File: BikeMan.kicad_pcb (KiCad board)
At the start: 2 copper layers, 78 parts, among them J1 USB_A_stacked, J10 HDMI_A_1.4, J2 USB_A_stacked, J4 Barrel_Jack, J5 PushConnector_8pos, J6 PushConnector_8pos, J7 PushConnector_8pos, J8 MagJack, J9 Micro_SD_Card_Det, Q1 AUIRF7316QTR, Q2 AUIRF7316QTR, Q3 AUIRF7316QTR, Q4 AUIRF7316QTR, U1 MCP2515, U2 MCP2551, U3 AP64501, U4 RT9742GGJ5, U5 NPIC6C596ADJ, U6 PCF8574DWR, U7 PCF85063A, U8 TUSB2046IBVF

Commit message: Added Daughter Card
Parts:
- removed R18, R19, R20, R21, R22, R23, R24, R25, R26, R27, R28, R29, R30, R31, R32, R33, R34, R35, R36, R37, R38: R, Resistor_SMD:R_0805_2012Metric
- removed U7: PCF85063A, Package_SO:SOIC-8_3.9x4.9mm_P1.27mm
- added H1: MountingHole_Pad, MountingHole:MountingHole_3.2mm_M3, F.Cu at (59.7, 38.1)
- added H2: MountingHole_Pad, MountingHole:MountingHole_3.2mm_M3, F.Cu at (203.2, 38.1)
- added H3: MountingHole_Pad, MountingHole:MountingHole_3.2mm_M3, F.Cu at (203.2, 152.4)
- added H4: MountingHole_Pad, MountingHole:MountingHole_3.2mm_M3, F.Cu at (59.7, 152.4)
- added J11: ExpansionSlotA, Connector_PinSocket_2.54mm:PinSocket_2x03_P2.54mm_Vertical, F.Cu at (128.3, 111.8)
- added J12: ExpansionSlotB, Connector_PinSocket_2.54mm:PinSocket_2x03_P2.54mm_Vertical, F.Cu at (87.6, 78.7)
- added J13: ExpansionSlotC, Connector_PinSocket_2.54mm:PinSocket_2x03_P2.54mm_Vertical, F.Cu at (128.3, 83.8)
- added J14: CAN_{OUT}, Connector_Molex:Molex_Micro-Fit_3.0_43045-0412_2x02_P3.00mm_Vertical, F.Cu at (66.0, 95.2)
- added J3: CAN_{IN}, Connector_Molex:Molex_Micro-Fit_3.0_43045-0412_2x02_P3.00mm_Vertical, F.Cu at (66.0, 83.6)
- added JP2: Jumper, Connector_PinHeader_2.54mm:PinHeader_1x02_P2.54mm_Vertical, F.Cu at (63.7, 69.5)
- J5: value PushConnector_8pos -> GPIO Outputs
- J6: value PushConnector_8pos -> GPIO Inputs
- J7: value PushConnector_8pos -> CAN / Power / GND
- R1, R2: moved to B.Cu
- R15, R16, R17: value R -> CTS-766161102GP; footprint Resistor_SMD:R_0805_2012Metric -> Package_SO:SOIC-16_3.9x9.9mm_P1.27mm; moved to B.Cu
- moved C8 283.9 mm to (79.2, 132.0)
- moved U3 283.9 mm to (71.6, 130.7)
- moved C7 276.8 mm to (79.2, 128.2)
- moved J4 275.7 mm to (71.1, 144.7)
- moved U1 241.4 mm to (78.7, 58.4), turned to -90 degrees
- moved R5 235.9 mm to (106.7, 54.6), turned to -90 degrees
- moved U2 234.6 mm to (99.7, 57.7), turned to -90 degrees
- moved JP1 228.6 mm to (108.0, 59.7), turned to 90 degrees
- moved JP4 184.4 mm to (73.5, 122.7)
- moved BT1 165.3 mm to (194.3, 81.3), turned to 90 degrees
- moved R4 154.4 mm to (68.6, 69.8), turned to -90 degrees
- moved D3 153.4 mm to (194.3, 96.5), turned to -90 degrees
- moved TP1 151.7 mm to (64.8, 59.7), turned to -90 degrees
- moved C2 140.3 mm to (91.4, 56.6), turned to 180 degrees
- moved R3 121.7 mm to (91.4, 61.0), turned to 180 degrees
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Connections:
- net /CAN_{H}_1 renamed /CAN_{H}
- net /CAN_{L}_1 renamed /CAN_{L}
- J8 pad 1: no_connect_196 -> no_connect_209
- J8 pad 8: no_connect_198 -> no_connect_211
- Module1 pad 10: no_connect_199 -> no_connect_212
- Module1 pad 102: no_connect_200 -> no_connect_213
- Module1 pad 104: no_connect_201 -> no_connect_214
- Module1 pad 106: no_connect_202 -> no_connect_215
- Module1 pad 109: no_connect_203 -> no_connect_216
- Module1 pad 110: no_connect_204 -> no_connect_217
- Module1 pad 111: no_connect_205 -> no_connect_218
- Module1 pad 112: no_connect_206 -> no_connect_219
- Module1 pad 115: no_connect_207 -> no_connect_220
- Module1 pad 116: no_connect_208 -> no_connect_221
- Module1 pad 117: no_connect_209 -> no_connect_222
- Module1 pad 118: no_connect_210 -> no_connect_223
- Module1 pad 12: no_connect_211 -> no_connect_224
- Module1 pad 121: no_connect_212 -> no_connect_225
- Module1 pad 122: no_connect_213 -> no_connect_226
- Module1 pad 123: no_connect_214 -> no_connect_227
- Module1 pad 124: no_connect_215 -> no_connect_228
- Module1 pad 127: no_connect_216 -> no_connect_229
- Module1 pad 128: no_connect_217 -> no_connect_230
- Module1 pad 129: no_connect_218 -> no_connect_231
- Module1 pad 130: no_connect_219 -> no_connect_232
- Module1 pad 133: no_connect_220 -> no_connect_233
- Module1 pad 134: no_connect_221 -> no_connect_234
- Module1 pad 135: no_connect_222 -> no_connect_235
- Module1 pad 136: no_connect_223 -> no_connect_236
- Module1 pad 139: no_connect_224 -> no_connect_237
- Module1 pad 140: no_connect_225 -> no_connect_238
- Module1 pad 141: no_connect_226 -> no_connect_239
- Module1 pad 142: no_connect_227 -> no_connect_240
- Module1 pad 143: no_connect_228 -> no_connect_241
- Module1 pad 145: no_connect_229 -> no_connect_242
- Module1 pad 146: no_connect_230 -> no_connect_243
- Module1 pad 147: no_connect_231 -> no_connect_244
- Module1 pad 148: no_connect_232 -> no_connect_245
- Module1 pad 149: no_connect_233 -> no_connect_246
- Module1 pad 152: no_connect_234 -> no_connect_247
- Module1 pad 154: no_connect_235 -> no_connect_248
- Module1 pad 157: no_connect_236 -> no_connect_249
- Module1 pad 158: no_connect_237 -> no_connect_250
- Module1 pad 159: no_connect_238 -> no_connect_251
- Module1 pad 160: no_connect_239 -> no_connect_252
- Module1 pad 163: no_connect_240 -> no_connect_253
- Module1 pad 164: no_connect_241 -> no_connect_254
- Module1 pad 165: no_connect_242 -> no_connect_255
- Module1 pad 166: no_connect_243 -> no_connect_256
- Module1 pad 169: no_connect_244 -> no_connect_257
- Module1 pad 171: no_connect_245 -> no_connect_258
- Module1 pad 175: no_connect_246 -> no_connect_259
- Module1 pad 177: no_connect_247 -> no_connect_260
- Module1 pad 181: no_connect_248 -> no_connect_261
- Module1 pad 183: no_connect_249 -> no_connect_262
- Module1 pad 187: no_connect_250 -> no_connect_263
- Module1 pad 189: no_connect_251 -> no_connect_264
- Module1 pad 19: no_connect_252 -> no_connect_265
- Module1 pad 193: no_connect_253 -> no_connect_266
- Module1 pad 195: no_connect_254 -> no_connect_267
- Module1 pad 3: no_connect_255 -> no_connect_268
- Module1 pad 5: no_connect_256 -> no_connect_269
- R15 pad 2: /GPIO/I_{1} -> Net-(R15-Pad16)
- R16 pad 1: /GPIO/I_{1} -> /GPIO/I_{3}
- R16 pad 2: GND -> /Input_{4}
- R17 pad 1: /Input_{2} -> +12V
- R17 pad 2: /GPIO/I_{2} -> +12V
- U1 pad 10: no_connect_257 -> no_connect_270
- U1 pad 11: no_connect_258 -> no_connect_271
- U1 pad 3: no_connect_259 -> no_connect_272
- U1 pad 4: no_connect_260 -> no_connect_273
- U1 pad 5: no_connect_261 -> no_connect_274
- U1 pad 6: no_connect_262 -> no_connect_275
- U2 pad 5: no_connect_263 -> no_connect_276
- U5 pad 9: no_connect_264 -> no_connect_277
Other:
- board outline added: 152.4 x 127 mm
- board text added: "Daughter Card"

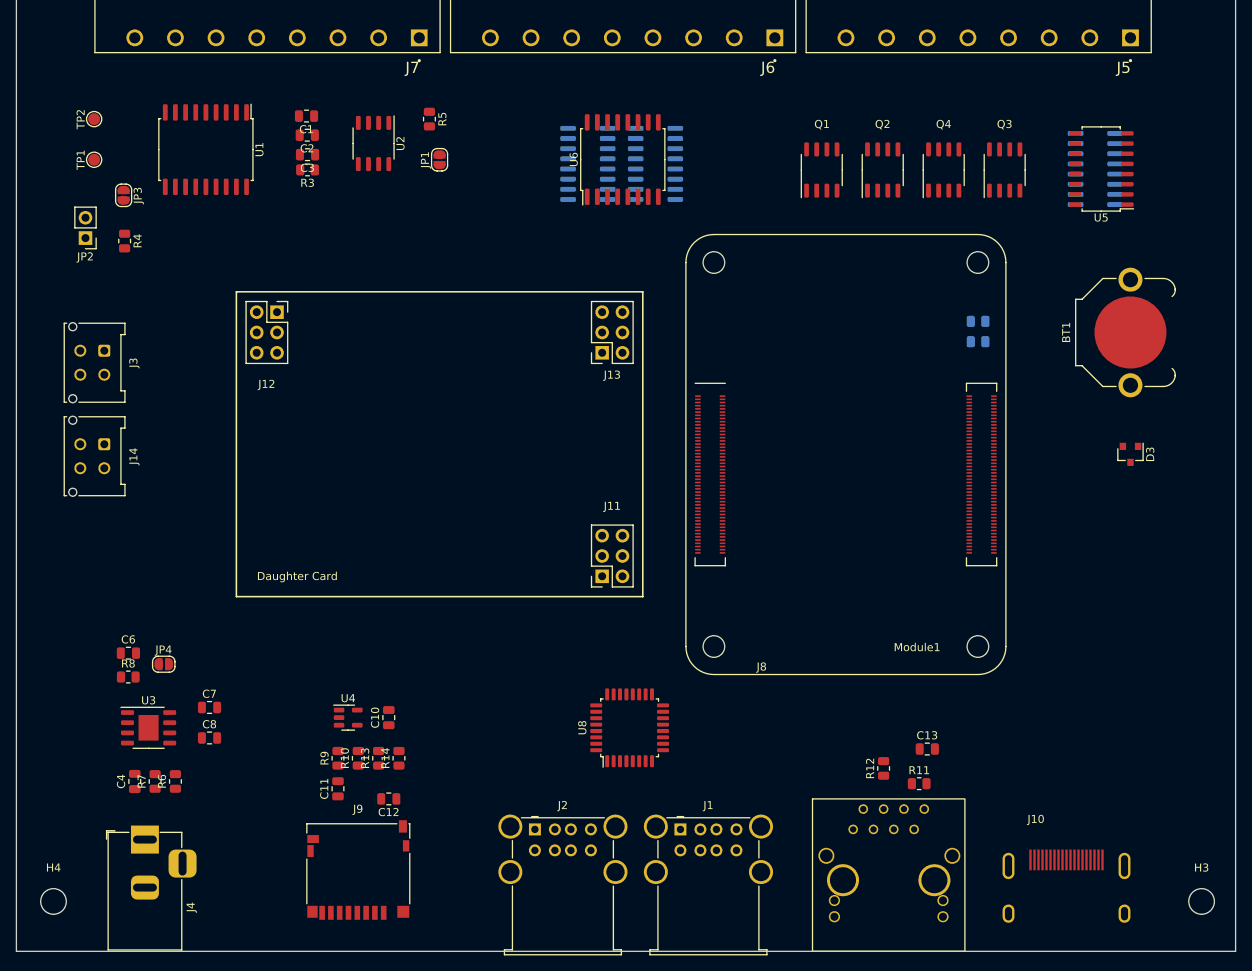
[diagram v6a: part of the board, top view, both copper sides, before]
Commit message: more layout: power supply and gpio
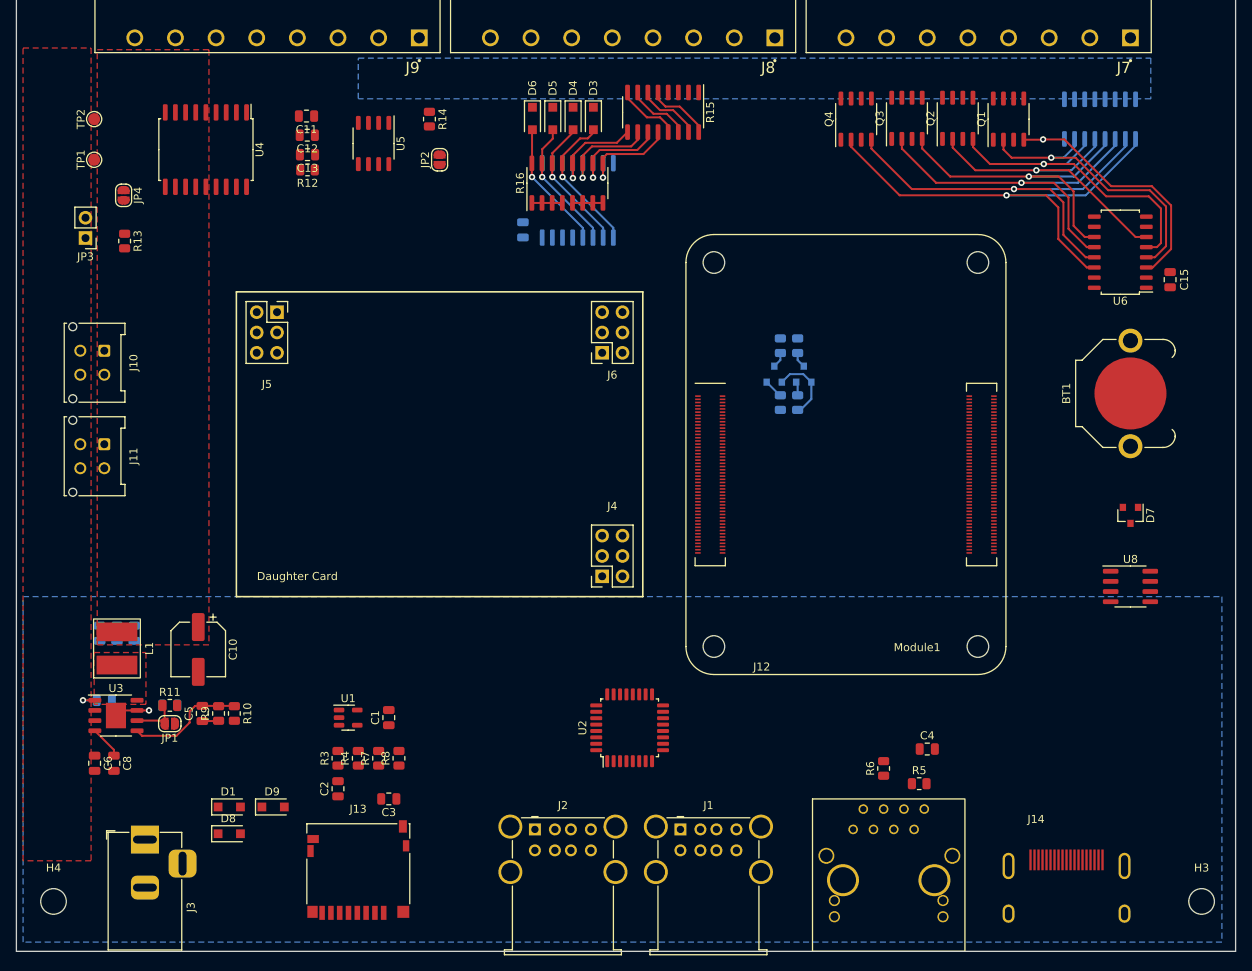
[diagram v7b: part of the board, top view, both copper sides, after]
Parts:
- added C10: 100uF, Capacitor_SMD:CP_Elec_6.3x5.9, F.Cu at (77.8, 120.9)
- added C14: C, Capacitor_SMD:C_0805_2012Metric, B.Cu at (118.4, 68.5)
- added C15: C, Capacitor_SMD:C_0805_2012Metric, F.Cu at (199.3, 74.7)
- added C16: 10uF, Capacitor_SMD:C_0805_2012Metric, B.Cu at (67.6, 118.9)
- added C17: 10uF, Capacitor_SMD:C_0805_2012Metric, B.Cu at (69.8, 118.9)
- added C18: 10uF, Capacitor_SMD:C_0805_2012Metric, B.Cu at (65.5, 118.9)
- added C6: 10uF, Capacitor_SMD:C_0805_2012Metric, F.Cu at (64.8, 135.1)
- added D1: Diode, Diode_SMD:D_SOD-123F, F.Cu at (81.7, 140.6)
- added D3: Diode, Diode_SMD:D_SOD-123F, F.Cu at (127.2, 54.5)
- added D4: Diode, Diode_SMD:D_SOD-123F, F.Cu at (124.6, 54.5)
- added D5: Diode, Diode_SMD:D_SOD-123F, F.Cu at (122.1, 54.5)
- added D6: Diode, Diode_SMD:D_SOD-123F, F.Cu at (119.6, 54.5)
- added D8: Diode, Diode_SMD:D_SOD-123F, F.Cu at (81.7, 143.9)
- added D9: Diode, Diode_SMD:D_SOD-123F, F.Cu at (87.1, 140.6)
- added L1: 3.3uH, Custom-Footprints:Bourns SRN6045Y Inductor, F.Cu at (67.6, 120.8)
- added Q5: DMN62D0U-7, Package_TO_SOT_SMD:SOT-23, B.Cu at (153.5, 86.5)
- added Q6: DMN62D0U-7, Package_TO_SOT_SMD:SOT-23, B.Cu at (149.8, 86.5)
- added R18: R, Resistor_SMD:R_0805_2012Metric, B.Cu at (152.7, 90.0)
- added R19: R, Resistor_SMD:R_0805_2012Metric, B.Cu at (150.5, 90.0)
- added U8: PCF85063A, Package_SO:SOIC-8_3.9x4.9mm_P1.27mm, F.Cu at (194.3, 113.0)
- C7: renamed from C6; moved to B.Cu
- C8: renamed from C7; value C -> 10nF
- C9: renamed from C8; value C -> 100nF; moved to B.Cu
- J10: renamed from J3; value CAN_{IN} -> Conn_01x04_Female
- J11: renamed from J14; value CAN_{OUT} -> Conn_01x04_Female
- J4: renamed from J11; value ExpansionSlotA -> Conn_01x06_Female
- J5: renamed from J12; value ExpansionSlotB -> Conn_01x06_Female
- J6: renamed from J13; value ExpansionSlotC -> Conn_01x06_Female
- J7: renamed from J5; value GPIO Outputs -> PushConnector_8pos
- J8: renamed from J6; value GPIO Inputs -> PushConnector_8pos
- J9: renamed from J7; value CAN / Power / GND -> PushConnector_8pos
- R15, R16: moved to F.Cu
- U7: renamed from U6; moved to B.Cu
- moved R2 24.7 mm to (150.5, 82.9), turned to -90 degrees
- moved Q1 24.2 mm to (179.1, 54.6)
- moved R1 22.8 mm to (152.7, 82.9), turned to -90 degrees
- moved C9 14.0 mm to (66.0, 127.3)
- moved C8 13.8 mm to (67.2, 135.1), turned to -90 degrees
- moved Q3 13.8 mm to (166.4, 54.5)
- moved R10 13.1 mm to (82.3, 128.9), turned to -90 degrees
- moved Q4 12.7 mm to (160.0, 54.6)
- moved C5 12.0 mm to (78.3, 128.9)
- moved Q2 11.4 mm to (172.7, 54.5)
- moved U6 10.7 mm to (193.0, 71.2)
- moved R9 10.1 mm to (80.3, 128.9)
- moved C7 8.33 mm to (74.2, 127.9), turned to 180 degrees
- moved BT1 7.62 mm to (194.3, 88.9)
- moved D7 7.62 mm to (194.3, 104.1)
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- renumbered C10 to C1, C1 to C11, C2 to C12, C3 to C13, C11 to C2, C12 to C3, C13 to C4, C4 to C5, D3 to D7, J8 to J12, J9 to J13, J10 to J14, J4 to J3, JP4 to JP1, JP1 to JP2, JP2 to JP3, JP3 to JP4, R7 to R10, R8 to R11, R3 to R12, R4 to R13, R5 to R14, R9 to R3, R10 to R4, R11 to R5, R12 to R6, R13 to R7, R14 to R8, R6 to R9, U4 to U1, U8 to U2, U1 to U4, U2 to U5, U5 to U6
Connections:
- net Net-(C8-Pad2) renamed /Power/SW
- net no_connect_206 renamed no_connect_210
- H1 pad 1: no_connect_205 -> no_connect_209
- H3 pad 1: no_connect_207 -> no_connect_211
- H4 pad 1: no_connect_208 -> no_connect_212
- J12 pad 1: no_connect_209 -> no_connect_213
- J12 pad 8: no_connect_211 -> no_connect_215
- J4 pad 4: /SCL -> /SDA_{5V}
- J4 pad 5: /SDA -> /SCL_{5V}
- Module1 pad 10: no_connect_212 -> no_connect_216
- Module1 pad 102: no_connect_213 -> no_connect_217
- Module1 pad 104: no_connect_214 -> no_connect_218
- Module1 pad 106: no_connect_215 -> no_connect_219
- Module1 pad 109: no_connect_216 -> no_connect_220
- Module1 pad 110: no_connect_217 -> no_connect_221
- Module1 pad 111: no_connect_218 -> no_connect_222
- Module1 pad 112: no_connect_219 -> no_connect_223
- Module1 pad 115: no_connect_220 -> no_connect_224
- Module1 pad 116: no_connect_221 -> no_connect_225
- Module1 pad 117: no_connect_222 -> no_connect_226
- Module1 pad 118: no_connect_223 -> no_connect_227
- Module1 pad 12: no_connect_224 -> no_connect_228
- Module1 pad 121: no_connect_225 -> no_connect_229
- Module1 pad 122: no_connect_226 -> no_connect_230
- Module1 pad 123: no_connect_227 -> no_connect_231
- Module1 pad 124: no_connect_228 -> no_connect_232
- Module1 pad 127: no_connect_229 -> no_connect_233
- Module1 pad 128: no_connect_230 -> no_connect_234
- Module1 pad 129: no_connect_231 -> no_connect_235
- Module1 pad 130: no_connect_232 -> no_connect_236
- Module1 pad 133: no_connect_233 -> no_connect_237
- Module1 pad 134: no_connect_234 -> no_connect_238
- Module1 pad 135: no_connect_235 -> no_connect_239
- Module1 pad 136: no_connect_236 -> no_connect_240
- Module1 pad 139: no_connect_237 -> no_connect_241
- Module1 pad 140: no_connect_238 -> no_connect_242
- Module1 pad 141: no_connect_239 -> no_connect_243
- Module1 pad 142: no_connect_240 -> no_connect_244
- Module1 pad 143: no_connect_241 -> no_connect_245
- Module1 pad 145: no_connect_242 -> no_connect_246
- Module1 pad 146: no_connect_243 -> no_connect_247
- Module1 pad 147: no_connect_244 -> no_connect_248
- Module1 pad 148: no_connect_245 -> no_connect_249
- Module1 pad 149: no_connect_246 -> no_connect_250
- Module1 pad 152: no_connect_247 -> no_connect_251
- Module1 pad 154: no_connect_248 -> no_connect_252
- Module1 pad 157: no_connect_249 -> no_connect_253
- Module1 pad 158: no_connect_250 -> no_connect_254
- Module1 pad 159: no_connect_251 -> no_connect_255
- Module1 pad 160: no_connect_252 -> no_connect_256
- Module1 pad 163: no_connect_253 -> no_connect_257
- Module1 pad 164: no_connect_254 -> no_connect_258
- Module1 pad 165: no_connect_255 -> no_connect_259
- Module1 pad 166: no_connect_256 -> no_connect_260
- Module1 pad 169: no_connect_257 -> no_connect_261
- Module1 pad 171: no_connect_258 -> no_connect_262
- Module1 pad 175: no_connect_259 -> no_connect_263
- Module1 pad 177: no_connect_260 -> no_connect_264
- Module1 pad 181: no_connect_261 -> no_connect_265
- Module1 pad 183: no_connect_262 -> no_connect_266
- Module1 pad 187: no_connect_263 -> no_connect_267
- Module1 pad 189: no_connect_264 -> no_connect_268
- Module1 pad 19: no_connect_265 -> no_connect_269
- Module1 pad 193: no_connect_266 -> no_connect_270
- Module1 pad 195: no_connect_267 -> no_connect_271
- Module1 pad 3: no_connect_268 -> no_connect_272
- Module1 pad 5: no_connect_269 -> no_connect_273
- Module1 pad 80: /SCL -> /SCL_{3.3V}
- Module1 pad 82: /SDA -> /SDA_{3.3V}
- Q1 pad 2: /GPIO/OUT_CTL_{1} -> /GPIO/OUT_CTL_{2}
- Q1 pad 4: /GPIO/OUT_CTL_{2} -> /GPIO/OUT_CTL_{1}
- Q1 pad 5: /OUT_{2} -> /OUT_{1}
- Q1 pad 7: /OUT_{1} -> /OUT_{2}
- Q2 pad 2: /GPIO/OUT_CTL_{3} -> /GPIO/OUT_CTL_{4}
- Q2 pad 4: /GPIO/OUT_CTL_{4} -> /GPIO/OUT_CTL_{3}
- Q2 pad 5: /OUT_{4} -> /OUT_{3}
- Q2 pad 7: /OUT_{3} -> /OUT_{4}
- Q3 pad 2: /GPIO/OUT_CTL_{5} -> /GPIO/OUT_CTL_{6}
- Q3 pad 4: /GPIO/OUT_CTL_{6} -> /GPIO/OUT_CTL_{5}
- Q3 pad 5: /OUT_{6} -> /OUT_{5}
- Q3 pad 7: /OUT_{5} -> /OUT_{6}
- Q4 pad 2: /GPIO/OUT_CTL_{7} -> /GPIO/OUT_CTL_{8}
- Q4 pad 4: /GPIO/OUT_CTL_{8} -> /GPIO/OUT_CTL_{7}
- Q4 pad 5: /OUT_{8} -> /OUT_{7}
- Q4 pad 7: /OUT_{7} -> /OUT_{8}
- R1 pad 1: +3V3 -> +5V
- R1 pad 2: /SDA -> /SDA_{5V}
- R15 pad 10: Net-(R15-Pad10) -> /GPIO/I_{3}
- R15 pad 11: GND -> /GPIO/I_{2}
- R15 pad 12: /GPIO/I_{2} -> /GPIO/I_{1}
- R15 pad 14: GND -> Net-(R15-Pad14)
- R15 pad 15: /GPIO/I_{1} -> Net-(R15-Pad15)
- R15 pad 2: Net-(R15-Pad16) -> /Input_{2}
- R15 pad 3: /GPIO/I_{1} -> /Input_{3}
- R15 pad 4: /Input_{2} -> /Input_{4}
- R15 pad 5: Net-(R15-Pad13) -> Net-(R15-Pad16)
- R15 pad 6: /GPIO/I_{2} -> Net-(R15-Pad15)
- R15 pad 7: /Input_{3} -> Net-(R15-Pad14)
- R15 pad 8: Net-(R15-Pad10) -> Net-(R15-Pad13)
- R15 pad 9: /GPIO/I_{3} -> /GPIO/I_{4}
- R16 pad 1: /GPIO/I_{3} -> +5V
- R16 pad 10: /GPIO/I_{7} -> /GPIO/I_{2}
- R16 pad 11: /GPIO/I_{6} -> /GPIO/I_{3}
- R16 pad 12: /GPIO/I_{5} -> /GPIO/I_{4}
- R16 pad 13: GND -> /GPIO/I_{5}
- R16 pad 14: /GPIO/I_{4} -> /GPIO/I_{6}
- R16 pad 15: Net-(R16-Pad15) -> /GPIO/I_{7}
- R16 pad 16: GND -> /GPIO/I_{8}
- R16 pad 2: /Input_{4} -> +5V
- R16 pad 3: Net-(R16-Pad15) -> +5V
- R16 pad 4: /GPIO/I_{4} -> +5V
- R16 pad 5: +5V -> GND
- R16 pad 6: +5V -> GND
- R16 pad 7: +5V -> GND
- R16 pad 8: +5V -> GND
- R16 pad 9: /GPIO/I_{8} -> /GPIO/I_{1}
- R2 pad 1: +3V3 -> +5V
- R2 pad 2: /SCL -> /SCL_{5V}
- U3 pad 9: (no net) -> GND
- U4 pad 10: no_connect_270 -> no_connect_274
- U4 pad 11: no_connect_271 -> no_connect_275
- U4 pad 3: no_connect_272 -> no_connect_276
- U4 pad 4: no_connect_273 -> no_connect_277
- U4 pad 5: no_connect_274 -> no_connect_278
- U4 pad 6: no_connect_275 -> no_connect_279
- U5 pad 5: no_connect_276 -> no_connect_280
- U6 pad 9: no_connect_277 -> no_connect_281
- U7 pad 10: /GPIO/I_{7} -> /GPIO/I_{6}
- U7 pad 11: /GPIO/I_{6} -> /GPIO/I_{7}
- U7 pad 12: /GPIO/I_{5} -> /GPIO/I_{8}
- U7 pad 14: /SCL -> /SCL_{5V}
- U7 pad 15: /SDA -> /SDA_{5V}
- U7 pad 16: +3V3 -> +5V
- U7 pad 4: /GPIO/I_{1} -> /GPIO/I_{4}
- U7 pad 5: /GPIO/I_{2} -> /GPIO/I_{3}
- U7 pad 6: /GPIO/I_{3} -> /GPIO/I_{2}
- U7 pad 7: /GPIO/I_{4} -> /GPIO/I_{1}
- U7 pad 9: /GPIO/I_{8} -> /GPIO/I_{5}
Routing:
- net /GPIO/OUT_CTL_{8}: track 0.00 -> 59.4 mm, vias 0 -> 1
- net /GPIO/OUT_CTL_{7}: track 0.00 -> 54.1 mm, vias 0 -> 1
- net /GPIO/OUT_CTL_{6}: track 0.00 -> 47.2 mm, vias 0 -> 1
- net /GPIO/OUT_CTL_{5}: track 0.00 -> 41.8 mm, vias 0 -> 1
- net /GPIO/OUT_CTL_{3}: track 0.00 -> 41.0 mm, vias 0 -> 1
- net /GPIO/OUT_CTL_{4}: track 0.00 -> 39.4 mm, vias 0 -> 1
- net /GPIO/OUT_CTL_{2}: track 0.00 -> 37.0 mm, vias 0 -> 1
- net /GPIO/OUT_CTL_{1}: track 0.00 -> 31.4 mm, vias 0 -> 1
- net /GPIO/I_{5}: track 0.00 -> 19.1 mm, vias 0 -> 1
- net /GPIO/I_{6}: track 0.00 -> 17.2 mm, vias 0 -> 1
- net /GPIO/I_{7}: track 0.00 -> 16.7 mm, vias 0 -> 1
- net /GPIO/I_{8}: track 0.00 -> 16.2 mm, vias 0 -> 1
- net /Power/feedback: track 0.00 -> 14.8 mm
- net /GPIO/I_{3}: track 0.00 -> 13.3 mm, vias 0 -> 1
- net /GPIO/I_{2}: track 0.00 -> 13.1 mm, vias 0 -> 1
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- added copper zone on B.Cu, net +12V
- added copper zone on F.Cu, net +12V
- added copper zone on F.Cu, net +5V
- added copper zone on F.Cu, net /Power/SW
- added copper zone on B.Cu, net GND
